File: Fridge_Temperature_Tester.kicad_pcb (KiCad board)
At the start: 2 copper layers, 100 x 50 mm, 2 parts, among them U1 DS18B20

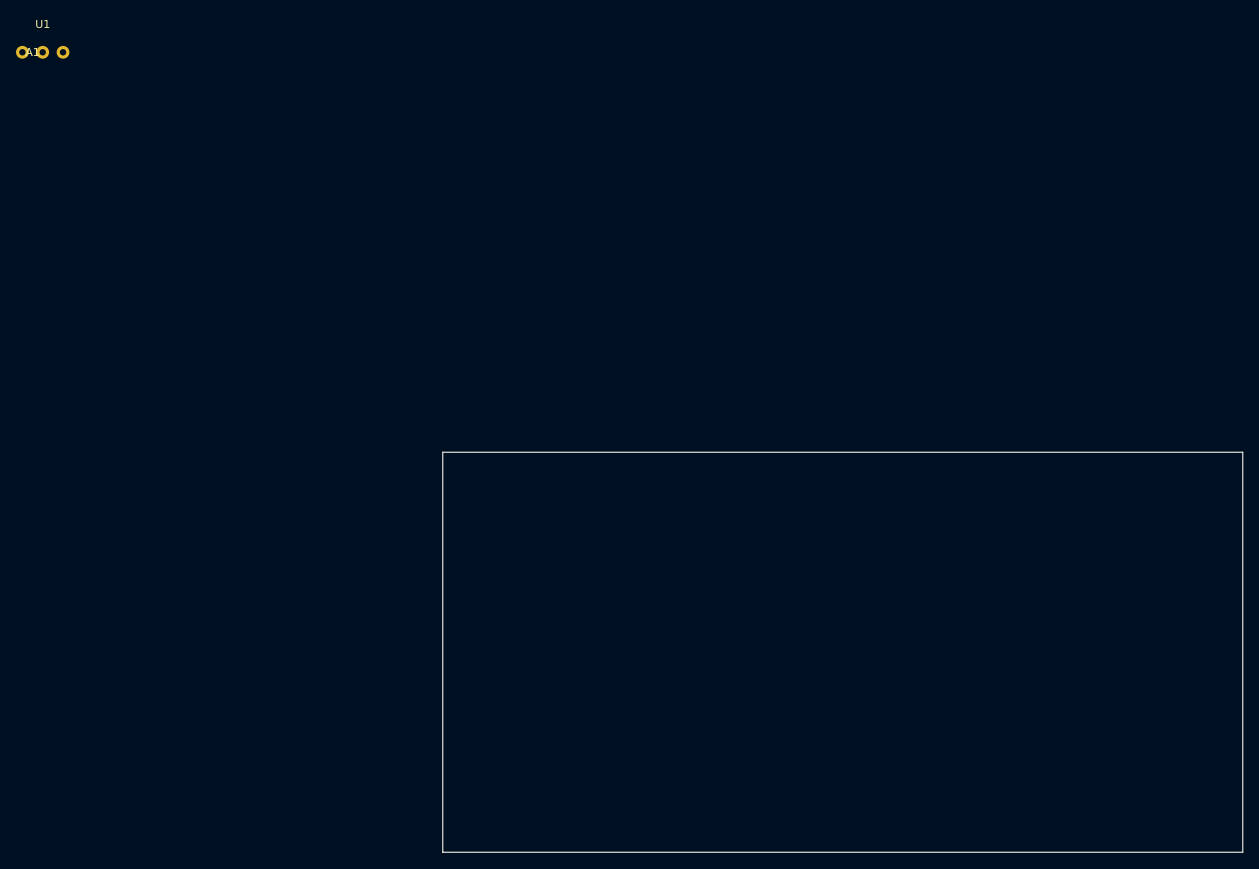
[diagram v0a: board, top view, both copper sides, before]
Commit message: Update PCB layout with component placement and board outline
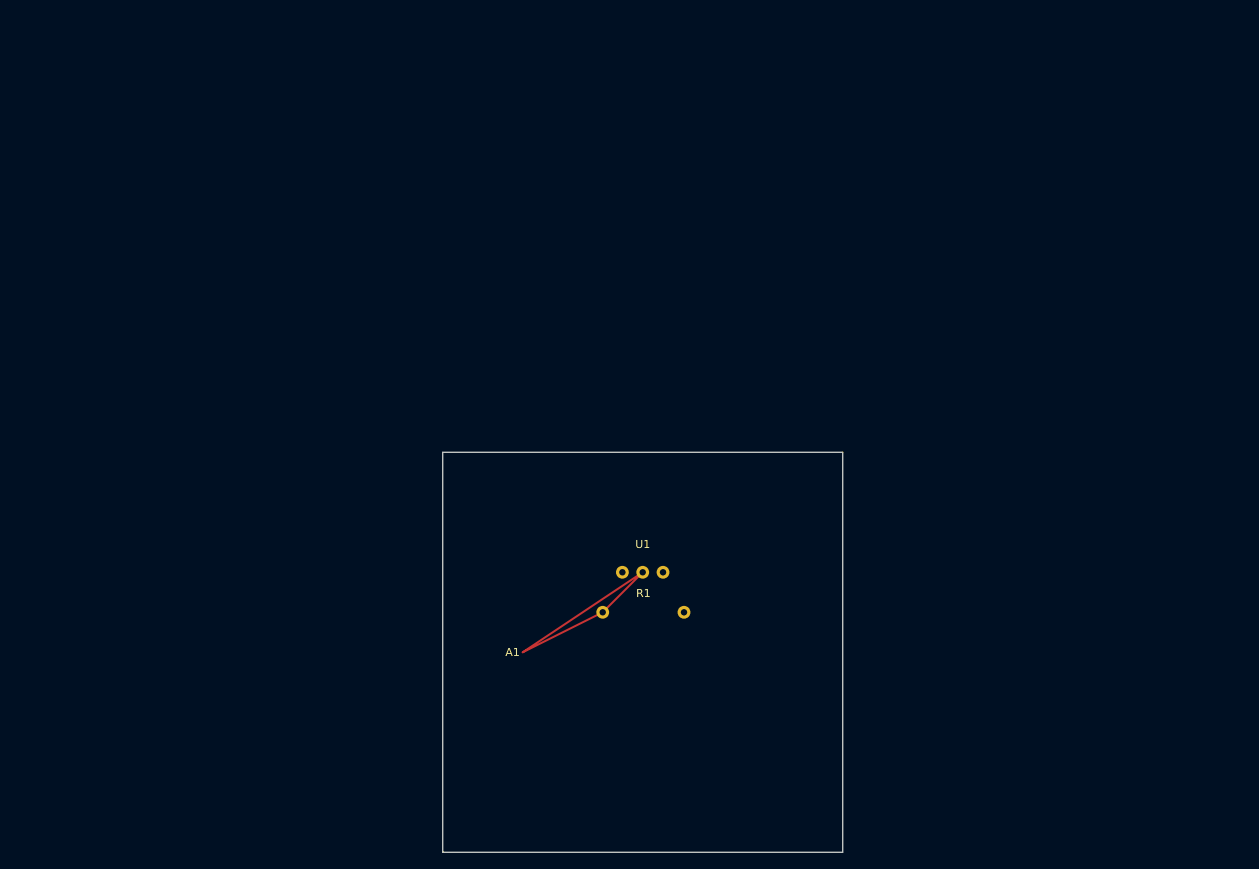
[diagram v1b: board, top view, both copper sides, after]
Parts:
- added R1: 4.7k, Resistor_THT:R_Axial_DIN0207_L6.3mm_D2.5mm_P10.16mm_Horizontal, F.Cu at (70.0, 70.0)
- moved U1 99.2 mm to (75.0, 65.0)
- moved A1 96.0 mm to (60.0, 75.0)
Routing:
- net GND: track 0.00 -> 18.0 mm
- net TEMP_SENSOR: track 0.00 -> 11.2 mm
- net +5V: track 0.00 -> 7.07 mm
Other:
- board size 100 x 50 mm -> 50 x 50 mm
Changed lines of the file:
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@@
   )
   (module "Package_TO_SOT_THT:TO-92_Inline" (layer "F.Cu")
+    (at 75 65)
     (descr "TO-92 leads in-line, narrow, oval pads")
     (tags "to-92 sc-43 sc-43a sot54 PA33 transistor")
@@
   )
   (module "Module:Arduino_Nano" (layer "F.Cu")
+    (at 60 75)
     (descr "Arduino Nano")
     (tags "Arduino Nano")
@@
     )
   )
-  (gr_line (start 50 50) (end 150 50) (layer "Edge.Cuts") (width 0.1))
-  (gr_line (start 150 50) (end 150 100) (layer "Edge.Cuts") (width 0.1))
-  (gr_line (start 150 100) (end 50 100) (layer "Edge.Cuts") (width 0.1))
+  (module "Resistor_THT:R_Axial_DIN0207_L6.3mm_D2.5mm_P10.16mm_Horizontal" (layer "F.Cu")
+    (at 70 70)
+    (descr "Resistor, Axial_DIN0207 series, Axial, Horizontal, pin pitch=10.16mm, 0.25W = 1/4W, length*diameter=6.3*2.5mm^2, http://cdn-reichelt.de/documents/datenblatt/B400/1_4W%23YAG.pdf")
+    (tags "Resistor Axial_DIN0207 series Axial Horizontal pin pitch 10.16mm 0.25W = 1/4W length 6.3mm diameter 2.5mm")
+    (attr through_hole)
+    (fp_text reference "R1" (at 5.08 -2.37) (layer "F.SilkS")
+      (effects (font (size 1 1) (thickness 0.15)))
+    )
+    (fp_text value "4.7k" (at 5.08 2.37) (layer "F.Fab")
+      (effects (font (size 1 1) (thickness 0.15)))
+    )
+    (pad "1" thru_hole circle (at 0 0) (size 1.6 1.6) (drill 0.8) (layers *.Cu *.Mask)
+      (net 2 "+5V"))
+    (pad "2" thru_hole oval (at 10.16 0) (size 1.6 1.6) (drill 0.8) (layers *.Cu *.Mask)
+      (net 3 "TEMP_SENSOR"))
+  )
+  (gr_line (start 50 50) (end 100 50) (layer "Edge.Cuts") (width 0.1))
+  (gr_line (start 100 50) (end 100 100) (layer "Edge.Cuts") (width 0.1))
+  (gr_line (start 100 100) (end 50 100) (layer "Edge.Cuts") (width 0.1))
   (gr_line (start 50 100) (end 50 50) (layer "Edge.Cuts") (width 0.1))
+  (segment (start 75 65) (end 60 75) (width 0.25) (layer "F.Cu") (net 1))
+  (segment (start 75 65) (end 70 70) (width 0.25) (layer "F.Cu") (net 2))
+  (segment (start 70 70) (end 60 75) (width 0.25) (layer "F.Cu") (net 3))
 )

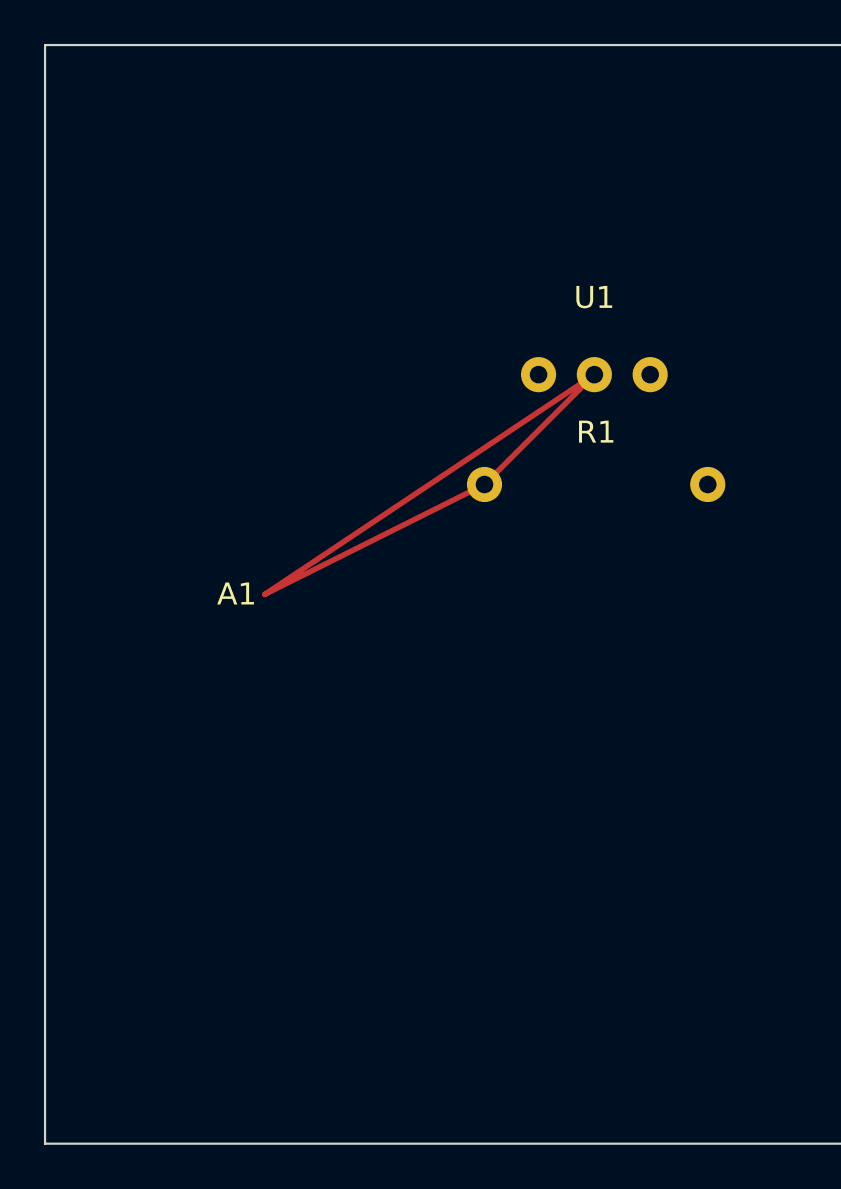
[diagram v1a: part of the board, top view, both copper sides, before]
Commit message: Refine PCB design with improved component footprints and simplified board outline
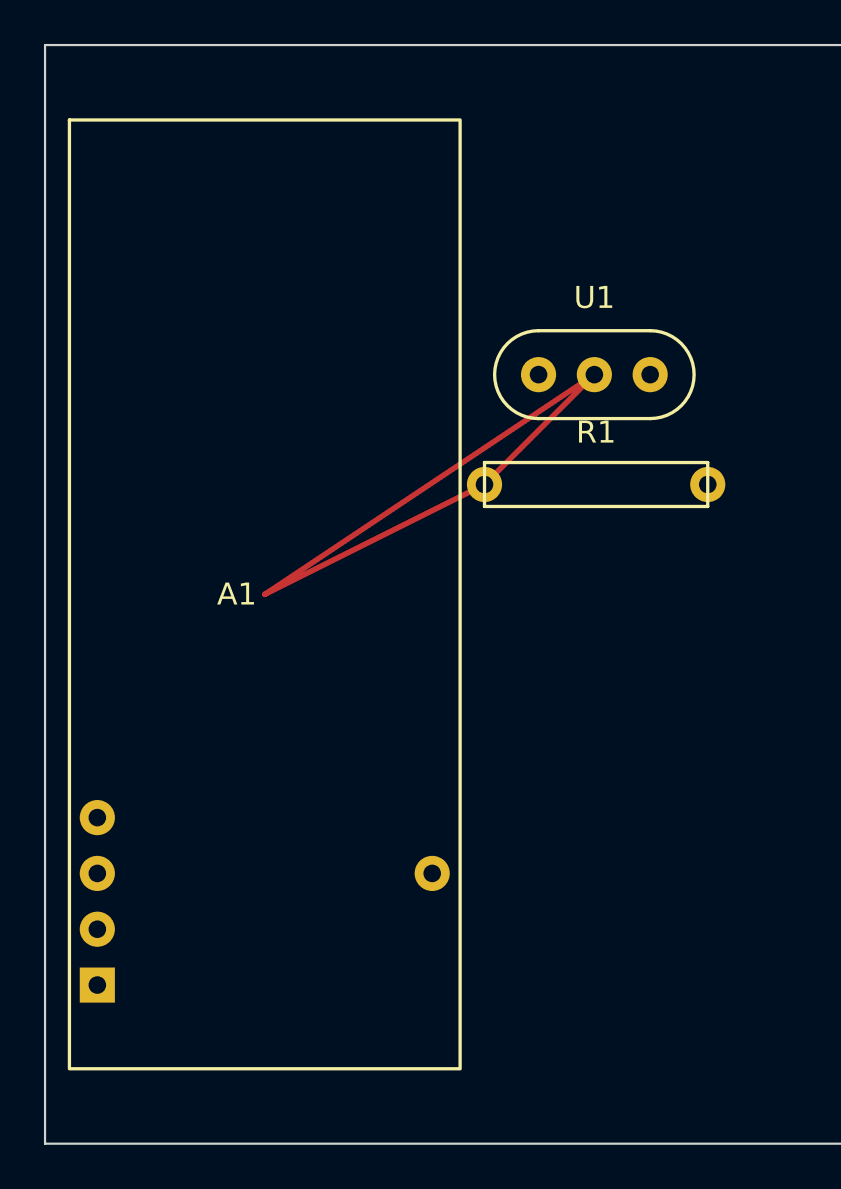
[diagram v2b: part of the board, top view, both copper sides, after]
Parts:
- R1: footprint Resistor_THT:R_Axial_DIN0207_L6.3mm_D2.5mm_P10.16mm_Horizontal -> Resistor_THT:R_Axial_DIN0207
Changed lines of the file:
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@@
   (setup
     (pad_to_mask_clearance 0.1)
+    (grid_origin 50 50)
     (pcbplotparams
       (layerselection 0x00010fc_ffffffff)
@@
     (add_net "TEMP_SENSOR")
   )
-  (module "Package_TO_SOT_THT:TO-92_Inline" (layer "F.Cu")
+  (footprint "Package_TO_SOT_THT:TO-92_Inline" (layer "F.Cu")
     (at 75 65)
-    (descr "TO-92 leads in-line, narrow, oval pads")
-    (tags "to-92 sc-43 sc-43a sot54 PA33 transistor")
+    (descr "TO-92 leads in-line")
     (attr through_hole)
     (fp_text reference "U1" (at 0 -3.5) (layer "F.SilkS")
@@
       (effects (font (size 1 1) (thickness 0.15)))
     )
+    (fp_line (start -2.54 -2) (end 2.54 -2) (layer "F.SilkS") (width 0.15))
+    (fp_line (start -2.54 2) (end 2.54 2) (layer "F.SilkS") (width 0.15))
+    (fp_arc (start -2.54 0) (end -2.54 -2) (angle -180) (layer "F.SilkS") (width 0.15))
+    (fp_arc (start 2.54 0) (end 2.54 2) (angle -180) (layer "F.SilkS") (width 0.15))
     (pad "1" thru_hole oval (at -2.54 0) (size 1.6 1.6) (drill 0.8) (layers *.Cu *.Mask)
       (net 1 "GND"))
@@
       (net 2 "+5V"))
   )
-  (module "Module:Arduino_Nano" (layer "F.Cu")
+  (footprint "Module:Arduino_Nano" (layer "F.Cu")
     (at 60 75)
     (descr "Arduino Nano")
-    (tags "Arduino Nano")
     (attr through_hole)
     (fp_text reference "A1" (at -1.27 0) (layer "F.SilkS")
@@
       (effects (font (size 1 1) (thickness 0.15)))
     )
+    (fp_rect (start -8.89 -21.59) (end 8.89 21.59) (layer "F.SilkS") (width 0.15))
+    (pad "1" thru_hole rect (at -7.62 17.78) (size 1.6 1.6) (drill 0.8) (layers *.Cu *.Mask)
+      (net 0 ""))
+    (pad "2" thru_hole circle (at -7.62 15.24) (size 1.6 1.6) (drill 0.8) (layers *.Cu *.Mask)
+      (net 0 ""))
+    (pad "3" thru_hole circle (at -7.62 12.7) (size 1.6 1.6) (drill 0.8) (layers *.Cu *.Mask)
+      (net 0 ""))
+    (pad "4" thru_hole circle (at -7.62 10.16) (size 1.6 1.6) (drill 0.8) (layers *.Cu *.Mask)
+      (net 1 "GND"))
+    (pad "27" thru_hole circle (at 7.62 12.7) (size 1.6 1.6) (drill 0.8) (layers *.Cu *.Mask)
+      (net 2 "+5V"))
   )
-  (module "Resistor_THT:R_Axial_DIN0207_L6.3mm_D2.5mm_P10.16mm_Horizontal" (layer "F.Cu")
+  (footprint "Resistor_THT:R_Axial_DIN0207" (layer "F.Cu")
     (at 70 70)
-    (descr "Resistor, Axial_DIN0207 series, Axial, Horizontal, pin pitch=10.16mm, 0.25W = 1/4W, length*diameter=6.3*2.5mm^2, http://cdn-reichelt.de/documents/datenblatt/B400/1_4W%23YAG.pdf")
-    (tags "Resistor Axial_DIN0207 series Axial Horizontal pin pitch 10.16mm 0.25W = 1/4W length 6.3mm diameter 2.5mm")
+    (descr "Resistor, Axial_DIN0207")
     (attr through_hole)
     (fp_text reference "R1" (at 5.08 -2.37) (layer "F.SilkS")
@@
       (effects (font (size 1 1) (thickness 0.15)))
     )
+    (fp_line (start 0 -1) (end 10.16 -1) (layer "F.SilkS") (width 0.15))
+    (fp_line (start 10.16 -1) (end 10.16 1) (layer "F.SilkS") (width 0.15))
+    (fp_line (start 10.16 1) (end 0 1) (layer "F.SilkS") (width 0.15))
+    (fp_line (start 0 1) (end 0 -1) (layer "F.SilkS") (width 0.15))
     (pad "1" thru_hole circle (at 0 0) (size 1.6 1.6) (drill 0.8) (layers *.Cu *.Mask)
       (net 2 "+5V"))
@@
       (net 3 "TEMP_SENSOR"))
   )
-  (gr_line (start 50 50) (end 100 50) (layer "Edge.Cuts") (width 0.1))
-  (gr_line (start 100 50) (end 100 100) (layer "Edge.Cuts") (width 0.1))
-  (gr_line (start 100 100) (end 50 100) (layer "Edge.Cuts") (width 0.1))
-  (gr_line (start 50 100) (end 50 50) (layer "Edge.Cuts") (width 0.1))
+  (gr_rect (start 50 50) (end 100 100) (layer "Edge.Cuts") (width 0.1))
   (segment (start 75 65) (end 60 75) (width 0.25) (layer "F.Cu") (net 1))
   (segment (start 75 65) (end 70 70) (width 0.25) (layer "F.Cu") (net 2))
